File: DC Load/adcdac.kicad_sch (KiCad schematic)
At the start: 27 parts, among them IC1 OPA277UA, IC3 DAC80501MDGST, U7 MCP3426, U8 OPA2182

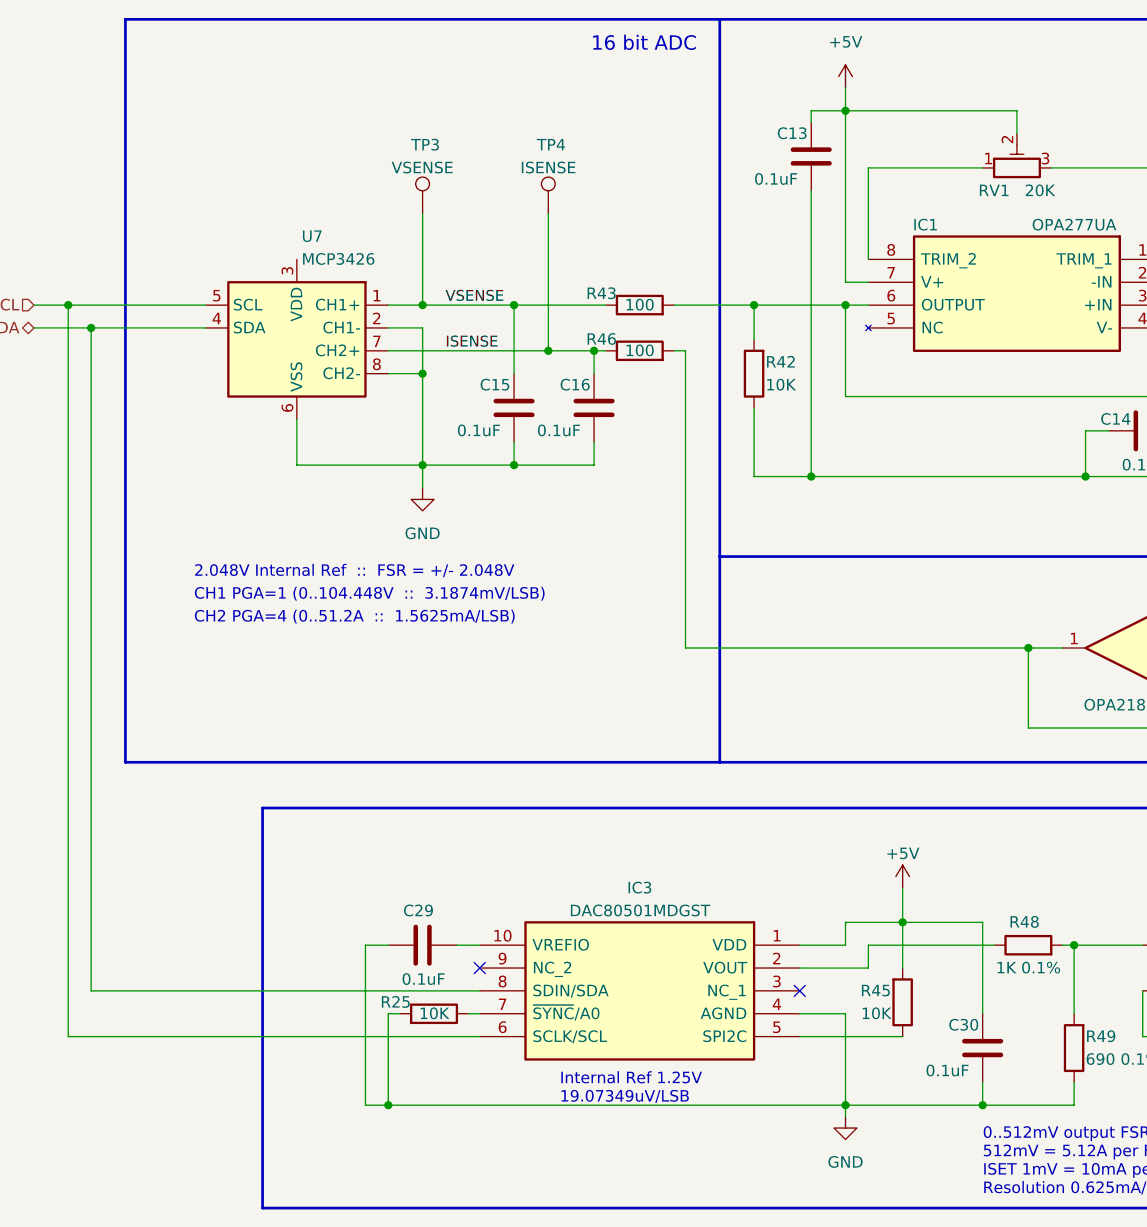
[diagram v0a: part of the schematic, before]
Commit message: Add power flags
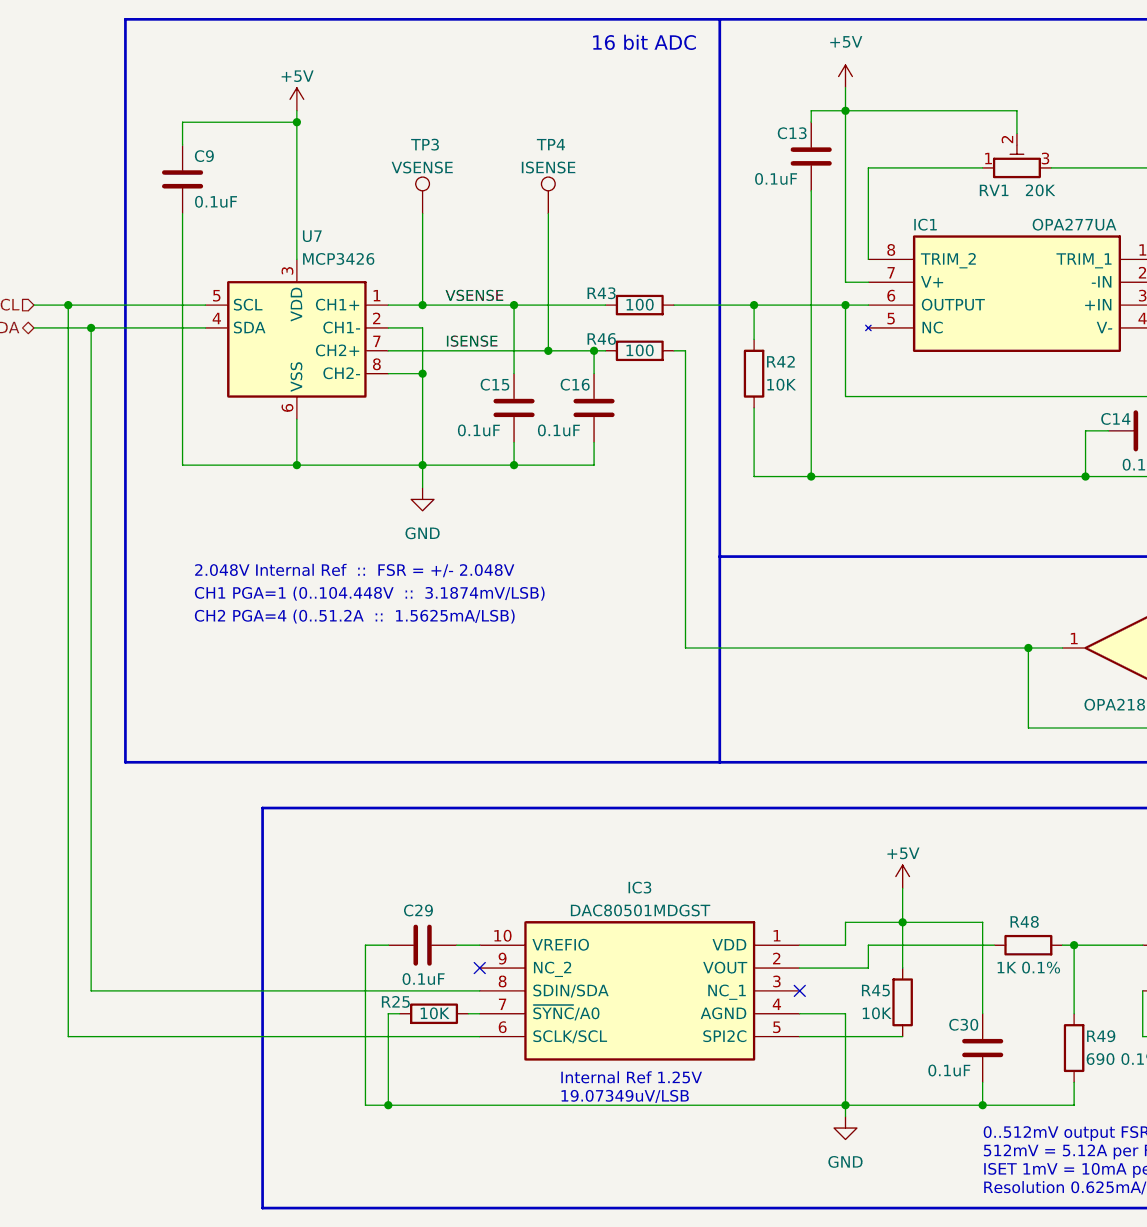
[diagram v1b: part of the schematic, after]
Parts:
- added C9: 0.1uF, symbol Device:C
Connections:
- net +5V: now also U7.3 (VDD), C9.1
- net GND: now also C9.2
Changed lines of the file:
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@@
   (junction (at 100.33 68.58) (diameter 0) (color 0 0 0 0)
   )
+  (junction (at 86.36 30.48) (diameter 0) (color 0 0 0 0)
+  )
   (junction (at 153.67 119.38) (diameter 0) (color 0 0 0 0)
+  )
+  (junction (at 86.36 68.58) (diameter 0) (color 0 0 0 0)
   )
   (junction (at 100.33 58.42) (diameter 0) (color 0 0 0 0)
@@
   (no_connect (at 106.68 124.46))
   (no_connect (at 142.24 127))
+  (wire (pts (xy 73.66 40.64) (xy 73.66 68.58))
+    (stroke (width 0) (type default) (color 0 0 0 0))
+  )
   (wire (pts (xy 93.98 121.92) (xy 96.52 121.92))
     (stroke (width 0) (type default) (color 0 0 0 0))
@@
     (stroke (width 0) (type default) (color 0 0 0 0))
   )
+  (wire (pts (xy 86.36 30.48) (xy 86.36 45.72))
+    (stroke (width 0) (type default) (color 0 0 0 0))
+  )
   (wire (pts (xy 100.33 40.64) (xy 100.33 50.8))
     (stroke (width 0) (type default) (color 0 0 0 0))
@@
     (stroke (width 0) (type default) (color 0 0 0 0))
   )
+  (wire (pts (xy 86.36 29.21) (xy 86.36 30.48))
+    (stroke (width 0) (type default) (color 0 0 0 0))
+  )
   (wire (pts (xy 147.32 119.38) (xy 153.67 119.38))
     (stroke (width 0) (type default) (color 0 0 0 0))
@@
     (stroke (width 0) (type default) (color 0 0 0 0))
   )
+  (wire (pts (xy 73.66 30.48) (xy 73.66 33.02))
+    (stroke (width 0) (type default) (color 0 0 0 0))
+  )
   (wire (pts (xy 143.51 29.21) (xy 147.32 29.21))
     (stroke (width 0) (type default) (color 0 0 0 0))
@@
     (stroke (width 0.3) (type default) (color 0 0 0 0))
   )
+  (wire (pts (xy 86.36 30.48) (xy 73.66 30.48))
+    (stroke (width 0) (type default) (color 0 0 0 0))
+  )
   (wire (pts (xy 170.18 35.56) (xy 182.88 35.56))
     (stroke (width 0) (type default) (color 0 0 0 0))
@@
   )
   (wire (pts (xy 147.32 121.92) (xy 147.32 119.38))
+    (stroke (width 0) (type default) (color 0 0 0 0))
+  )
+  (wire (pts (xy 73.66 68.58) (xy 86.36 68.58))
     (stroke (width 0) (type default) (color 0 0 0 0))
   )
@@
     (pin "2")
   )
+  (symbol (lib_id "power:+5V") (at 86.36 29.21 0) (mirror y) (unit 1)
+    (in_bom yes) (on_board yes)
+    (property "Reference" "#PWR0101" (id 0) (at 86.36 33.02 0)
+      (effects (font (size 1.27 1.27)) hide)
+    )
+    (property "Value" "+5V" (id 1) (at 86.36 25.4 0))
+    (property "Footprint" "" (id 2) (at 86.36 29.21 0)
+      (effects (font (size 1.27 1.27)) hide)
+    )
+    (property "Datasheet" "" (id 3) (at 86.36 29.21 0)
+      (effects (font (size 1.27 1.27)) hide)
+    )
+    (pin "1")
+  )
   (symbol (lib_id "power:GND") (at 100.33 71.12 0) (unit 1)
     (in_bom yes) (on_board yes) (fields_autoplaced)
@@
     )
     (property "Datasheet" "~" (id 3) (at 124.46 50.8 0)
+      (effects (font (size 1.27 1.27)) hide)
+    )
+    (pin "1")
+    (pin "2")
+  )
+  (symbol (lib_id "Device:C") (at 73.66 36.83 0) (unit 1)
+    (in_bom yes) (on_board yes)
+    (property "Reference" "C9" (id 0) (at 74.93 34.29 0)
+      (effects (font (size 1.27 1.27)) (justify left))
+    )
+    (property "Value" "0.1uF" (id 1) (at 74.93 39.37 0)
+      (effects (font (size 1.27 1.27)) (justify left))
+    )
+    (property "Footprint" "" (id 2) (at 74.6252 40.64 0)
+      (effects (font (size 1.27 1.27)) hide)
+    )
+    (property "Datasheet" "~" (id 3) (at 73.66 36.83 0)
       (effects (font (size 1.27 1.27)) hide)
     )
@@
       (effects (font (size 1.27 1.27)) (justify left))
     )
-    (property "Value" "0.1uF" (id 1) (at 156.21 135.89 0)
-      (effects (font (size 1.27 1.27)) (justify left))
+    (property "Value" "0.1uF" (id 1) (at 161.29 135.89 0)
+      (effects (font (size 1.27 1.27)) (justify right))
     )
     (property "Footprint" "" (id 2) (at 163.5252 137.16 0)

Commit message: update
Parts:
- removed C29: 0.1uF, symbol Device:C
- added C12: 0.1uF, symbol Device:C
- R48: value 1K 0.1% -> 3K 0.05%
- R49: value 690 0.1% -> 1K 0.05%
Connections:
- net GND: now also C12.2
- net +2.048V: now reaches IC3.10 (VREFIO)
- net +2.048V: now also C12.1
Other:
- note added: "External Ref 2.048V"
- note added: "VREFIO < 0.5*VDD (VDD >= 3.3V)"
- note removed: "Internal Ref 1.25V 19.07349uV/LSB"
- moved on the sheet: C14, C30, IC3, R25, R44, R45, R48, R49, U8A, U8B

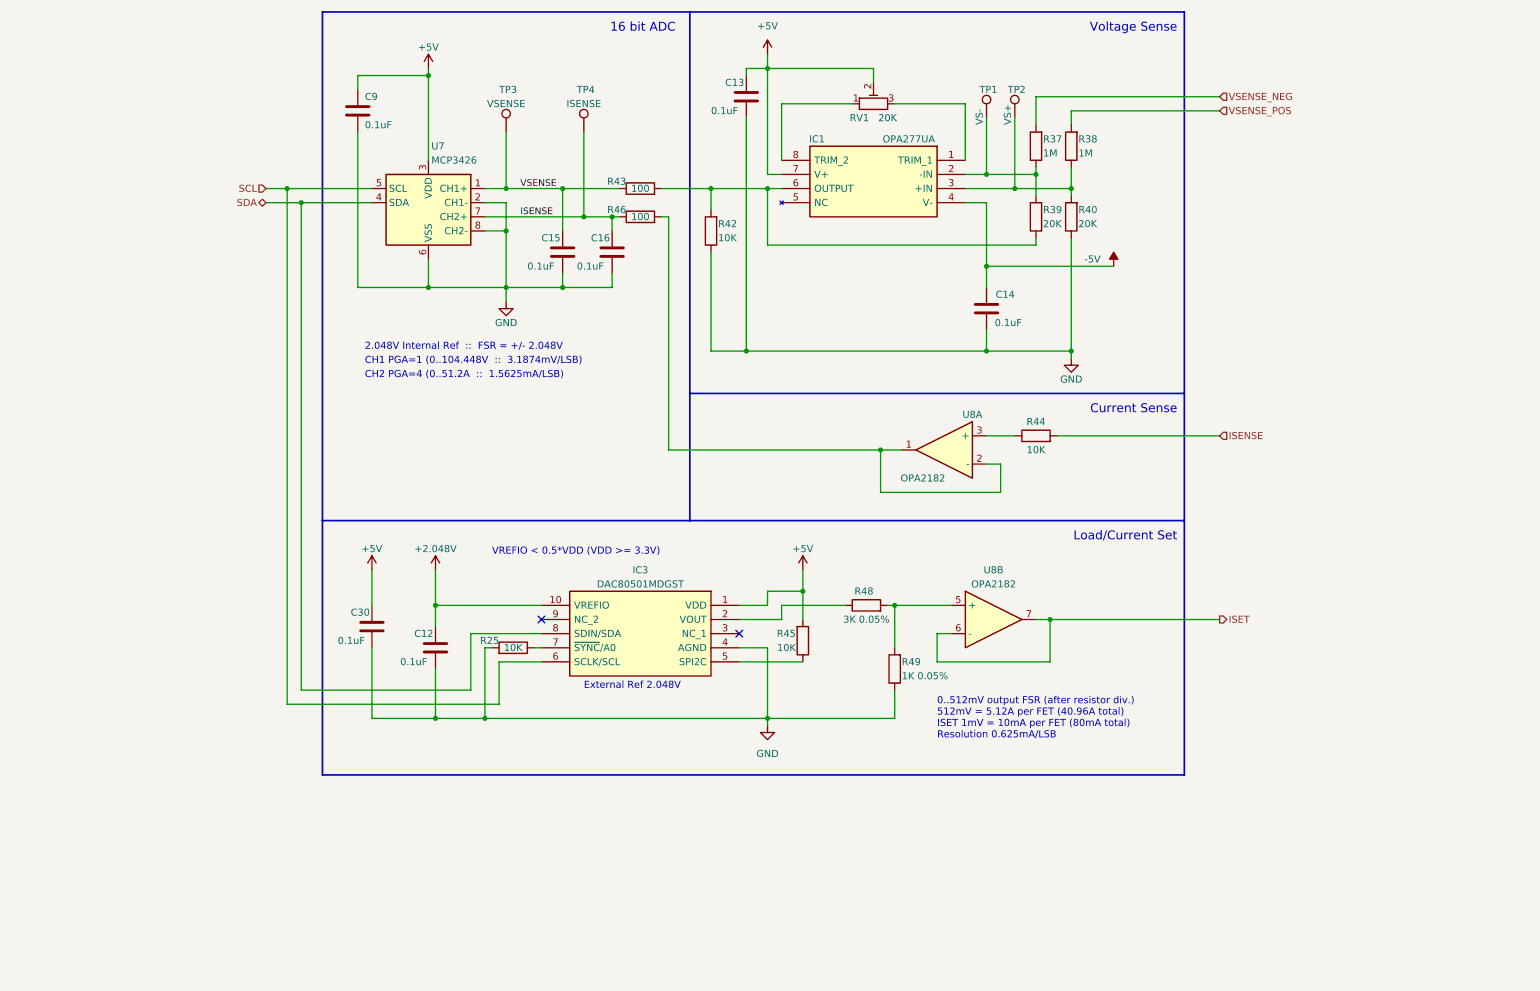
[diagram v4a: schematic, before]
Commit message: Swap DAC to MAX5217
Allows use of 2.048v ref with 3.3V VDD
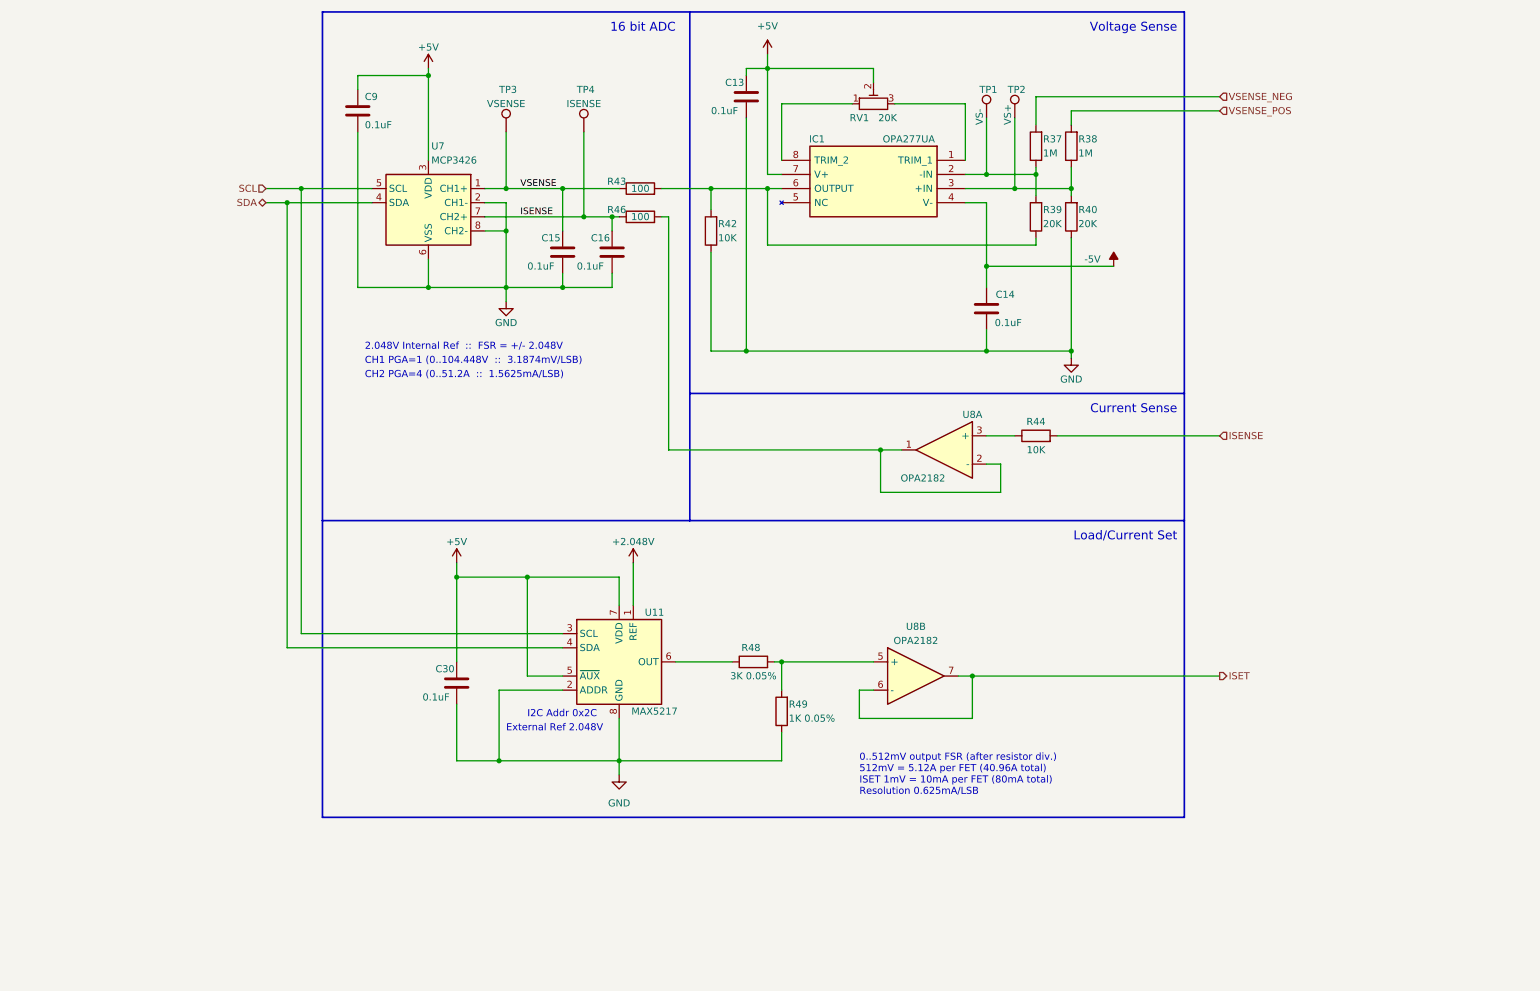
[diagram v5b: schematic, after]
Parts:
- removed C12: 0.1uF, symbol Device:C
- removed IC3: DAC80501MDGST, SOP50P490X110-10N, symbol SamacSys_Parts:DAC80501MDGST
- removed R25, R45: 10K, symbol Device:R
- added U11: MAX5217, Package_SO:MSOP-8_3x3mm_P0.65mm, symbol Analog_DAC:MAX5217
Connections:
- net +2.048V: now also U11.1 (REF)
- net +5V: now also U11.5 (~{AUX}), U11.7 (VDD)
- net GND: now also U11.2 (ADDR), U11.8 (GND)
- net SCL: now also U11.3 (SCL)
- net SDA: now also U11.4 (SDA)
- net at R48.1: now also U11.6 (OUT)
- no-connect marks 2 -> 0
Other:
- note added: "I2C Addr 0x2C"
- note removed: "VREFIO < 0.5*VDD (VDD >= 3.3V)"
- moved on the sheet: C30, R48, R49, U8B

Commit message: Swap to ADS131 ADC
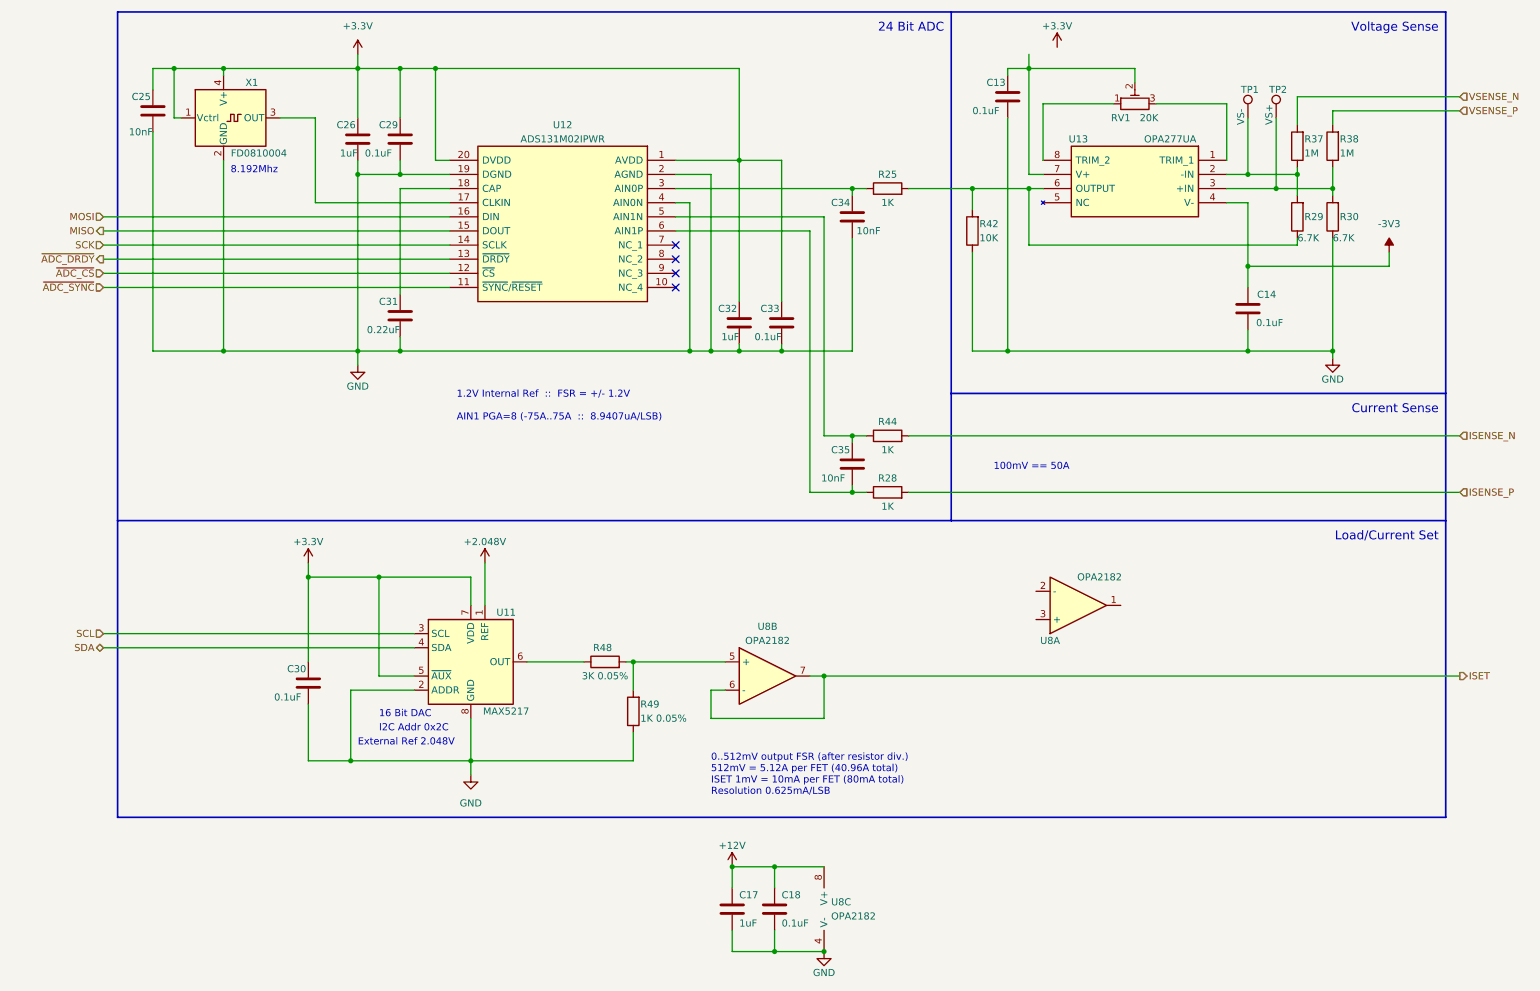
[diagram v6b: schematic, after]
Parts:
- removed C15, C16, C9: 0.1uF, symbol Device:C
- removed R39, R40: 20K, symbol Device:R
- removed R43, R46: 100, symbol Device:R
- removed TP3: VSENSE, symbol Connector:TestPoint
- removed TP4: ISENSE, symbol Connector:TestPoint
- removed U7: MCP3426, symbol Analog_ADC:MCP3426-xSN
- added C17, C26, C32: 1uF, symbol Device:C
- added C18, C29, C33: 0.1uF, symbol Device:C
- added C25, C34, C35: 10nF, symbol Device:C
- added C31: 0.22uF, symbol Device:C
- added R25, R28: 1K, symbol Device:R
- added R29, R30: 6.7K, symbol Device:R
- added U12: ADS131M02IPWR, SOP65P640X120-20N, symbol SamacSys_Parts:ADS131M02IPWR
- added unit 3 of U8
- added X1: FD0810004, symbol Oscillator:DFA-S15
- R44: value 10K -> 1K
- renumbered IC1 to U13
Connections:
- net GND: now also C17.2, C18.2, C25.2, C26.2, C29.2, C31.2, C32.2, C33.2, C34.2, R30.1, U12.19 (DGND), U12.2 (AGND), U12.4 (AIN0N), U8.4 (V-), X1.2 (GND)
- net at R42.2, U13.6 (OUTPUT): now also R25.2, R29.1
- net at R37.1, TP1.1, U13.2 (-IN): now also R29.2
- net at U8.1: no longer U8.2 (-)
- net at U8.3 (+): no longer R44.1
- net at R38.1, TP2.1, U13.3 (+IN): now also R30.2
- net +5V: no longer names the net of C13.1, RV1.2, U13.7 (V+)
- net +5V: no longer C30.1, U11.5 (~{AUX}), U11.7 (VDD)
- net -5V renamed -3V3
- net ISENSE renamed ISENSE_N
- net VSENSE_NEG renamed VSENSE_N
- net VSENSE_POS renamed VSENSE_P
- new net: U12.17 (CLKIN), X1.3 (OUT)
- new net: C35.1, R44.1, U12.5 (AIN1N)
- new net: C31.1, U12.18 (CAP)
- new net: C35.2, R28.1, U12.6 (AIN1P)
- new net: C34.1, R25.1, U12.3 (AIN0P)
- new net +12V: C17.1, C18.1, U8.8 (V+)
- new net +3V3: C25.1, C26.1, C29.1, C30.1, C32.1, C33.1, U11.5 (~{AUX}), U11.7 (VDD), U12.1 (AVDD), U12.20 (DVDD), X1.1 (Vctrl), X1.4 (V+)
- new net ISENSE_P: R28.2
- new net MISO: U12.15 (DOUT)
- new net MOSI: U12.16 (DIN)
- new net SCK: U12.14 (SCLK)
- new net ~{ADC_CS}: U12.12 (~{CS})
- new net ~{ADC_DRDY}: U12.13 (~{DRDY})
- new net ~{ADC_SYNC}: U12.11 (~{SYNC}/~{RESET})
- no-connect marks 0 -> 4
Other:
- note added: "1.2V Internal Ref :: FSR = +/- 1.2V AIN1 PGA=8 (-75A..75A :: 8.9407uA/LSB)"
- note added: "100mV == 50A"
- note added: "16 Bit DAC"
- note added: "24 Bit ADC"
- note added: "8.192Mhz"
- note removed: "16 bit ADC"
- note removed: "2.048V Internal Ref :: FSR = +/- 2.048V"
- note removed: "CH1 PGA=1 (0..104.448V :: 3.1874mV/LSB)"
- note removed: "CH2 PGA=4 (0..51.2A :: 1.5625mA/LSB)"
- moved on the sheet: C13, C14, C30, R37, R38, R42, R44, R48, R49, RV1, TP1, TP2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
